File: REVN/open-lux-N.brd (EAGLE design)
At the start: 53 x 68.6 mm, 71 parts, among them IC2 MCP73831, IC3 ATMEGA32U4-AU, IC4 MCP1700-33, J1 AYZ0202, Q1 BSS123, Q4 BSS123, T1 FDN340P, T2 FDN340P, X2 USBSMD, X3 8MHz

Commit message: prettified
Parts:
- moved RIR3 16.1 mm to (3.30, 57.7), turned to 0 degrees
- moved RIR4 15.2 mm to (3.30, 54.9), turned to 180 degrees
- moved Q4 9.66 mm to (22.6, 57.1), turned to 180 degrees
- moved C1 9.21 mm to (19.3, 65.8), turned to 270 degrees
- moved U$7 8.64 mm to (3.56, 47.0)
- moved RC 4.32 mm to (19.3, 61.0), turned to 270 degrees
- moved EEPRM 3.45 mm to (25.7, 65.0), turned to 270 degrees
- moved T1 3.30 mm to (20.8, 11.7), turned to 180 degrees
- moved B1 3.05 mm to (12.7, 64.5)
- moved RD-1 2.97 mm to (37.6, 26.9)
- moved C5 2.40 mm to (44.5, 53.8)
- moved CN1 2.30 mm to (3.81, 35.6)
- moved T2 1.93 mm to (26.2, 11.4)
- moved IC3 1.55 mm to (10.9, 22.9)
- moved C7 1.37 mm to (23.1, 18.0)
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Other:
- board text added: "LUX"
- board text added: "OPEN-"
- board text added: "PUBLICLAB"

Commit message: update
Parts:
- removed J1: AYZ0202, SparkFunNew:AYZ0202
- added J2: EG1206, adafruit:EG1206
- moved C3 42.3 mm to (8.89, 25.7)
- moved IC4 38.2 mm to (8.64, 32.0)
- moved C2 37.0 mm to (8.89, 28.4), turned to 180 degrees
- moved C6 24.2 mm to (2.54, 15.7), turned to 270 degrees
- moved CHARGE 18.2 mm to (32.5, 59.4), turned to 90 degrees
- moved Q1 17.4 mm to (14.2, 31.2)
- moved C7 16.7 mm to (6.60, 15.5)
- moved X3 15.9 mm to (5.08, 20.6), turned to 0 degrees
- moved C9 14.2 mm to (7.11, 2.03)
- moved RE1 9.96 mm to (33.0, 56.6), turned to 180 degrees
- moved RIR3 8.92 mm to (6.35, 66.0), turned to 90 degrees
- moved CN1 8.39 mm to (3.56, 43.9)
- moved IC3 8.18 mm to (18.3, 19.3), turned to 270 degrees
- moved U$7 7.37 mm to (3.56, 54.4)
- moved RIR4 7.18 mm to (4.32, 62.0)
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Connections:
- removed net N$1: J1.3, J1.6
- new net N$16: J2.2
- net VBAT: no longer J1.2, J1.5
- net VDD: now also J2.3; no longer J1.1, J1.4
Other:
- board text added: "PUBLICLAB.ORG"
- board text removed: "PUBLICLAB"

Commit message: update
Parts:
- removed RE2, RE3, RE6: 1.5K, rcl:R0805
- added IRR1, IRR2, IRR5: 1.5K, rcl:R0805
- moved RIR4 11.5 mm to (3.56, 50.5)
- moved IC4 4.38 mm to (7.87, 36.3)
- moved U$7 3.56 mm to (3.56, 57.9)
- moved C2 2.34 mm to (7.37, 30.2), turned to 270 degrees
- moved LUXRGB2 2.18 mm to (42.9, 49.8)
- moved C3 1.55 mm to (7.37, 25.4), turned to 90 degrees
- moved J2 0.80 mm to (2.79, 31.0)
- moved LUXNIR1 0.80 mm to (39.1, 55.4)
- moved B1 0.76 mm to (13.5, 64.5)
- moved C5 0.76 mm to (45.2, 55.6)
- moved RIR3 0.76 mm to (7.11, 66.0)
- moved C4 0.57 mm to (27.2, 36.3), turned to 0 degrees
- moved CHARGE 0.57 mm to (32.0, 59.7)
- moved IR4 0.57 mm to (22.1, 47.2)
- moved EEPRM 0.51 mm to (28.4, 64.8)
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- renumbered RE4 to IRR3, RE5 to IRR4
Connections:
- removed net N$8: IR5.C
- removed net VCC1: RE6.2
- net N$11: now also IRR1.1; no longer RE3.1
- net N$13: now also IRR2.1; no longer RE2.1
- net N$18: now also IRR5.1; no longer RE6.1
- net N$9: now also IR5.C
- net VCC: now also IRR1.2, IRR2.2, IRR5.2; no longer RE2.2, RE3.2

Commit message: update
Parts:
- moved RC 2.34 mm to (22.6, 62.7)
- moved C1 1.93 mm to (22.4, 66.5), turned to 180 degrees
- moved EEPRM 1.80 mm to (30.2, 65.0)
- moved U$1 1.30 mm to (41.1, 63.5)
- moved B1 1.02 mm to (14.5, 64.5)
- moved C5 0.57 mm to (45.0, 55.1)
- moved RIR3 0.25 mm to (6.86, 66.0), turned to 180 degrees

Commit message: update
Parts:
- removed U$7: M04X2, SparkFun-Connectors:2X4
- added JP2: M05X2NO_SILK, SparkFun-Connectors:2X5_NOSILK
- moved RIR4 19.3 mm to (20.6, 59.7)
- moved C6 4.83 mm to (2.54, 20.6)
- moved C7 4.07 mm to (2.54, 15.7), turned to 270 degrees
- moved X3 2.75 mm to (6.60, 18.3), turned to 90 degrees
- moved C3 1.85 mm to (7.87, 27.2)
- moved C2 1.61 mm to (7.87, 31.8)
- moved Q4 1.48 mm to (22.4, 56.4)
- moved CN1 1.30 mm to (3.81, 45.2)
- moved IRG 1.14 mm to (13.0, 58.7)
- moved IRL 1.14 mm to (10.4, 56.1)
- moved EEPRM 1.05 mm to (31.2, 64.8)
- moved IC3 1.05 mm to (17.3, 19.6), turned to 225 degrees
- moved C1 1.05 mm to (23.4, 66.3)
- moved J2 0.92 mm to (3.30, 31.8)
- moved IC4 0.92 mm to (8.64, 36.8)
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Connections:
- net VDD renamed N$1
- removed net N$16: J2.2
- net A0: now also JP2.6; no longer NKA.5, NKA1.6
- net A1: now also B2.1, JP2.8; no longer NKA.4, NKA1.5
- net A2: now also B3.1, JP2.10; no longer NKA.3
- net A3: now also B1.1; no longer NKA.1, NKA1.2
- net A4: now also NKA.1, NKA1.2; no longer B2.1
- net D4: now also NKA.3, NKA1.4; no longer U$7.5
- net D8: now also NKA.5, NKA1.6; no longer B1.1
- net D9: now also NKA.4, NKA1.5; no longer B3.1
- net GND: now also JP2.9; no longer U$7.4
- net RXD: now also JP2.2; no longer U$7.8
- net SCL: now also JP2.3; no longer U$7.3
- net SDA: now also JP2.1; no longer U$7.1
- net TXD: now also JP2.4; no longer U$7.6
- net VBAT: now also J2.2
- net VBUS: now also JP2.5; no longer U$7.7
- net VCC: now also JP2.7
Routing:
- net GND: track 0.00 -> 481.6 mm, vias 0 -> 13
- net VCC: track 0.00 -> 370.3 mm, vias 0 -> 18
- net VBUS: track 0.00 -> 153.1 mm, vias 0 -> 7
- net SCL: track 0.00 -> 129.1 mm, vias 0 -> 7
- net A2: track 0.00 -> 121.5 mm, vias 0 -> 4
- net A1: track 0.00 -> 116.2 mm, vias 0 -> 3
- net VBAT: track 0.00 -> 106.0 mm, vias 0 -> 3
- net SDA: track 0.00 -> 104.5 mm, vias 0 -> 8
- net D5: track 0.00 -> 74.5 mm, vias 0 -> 2
- net A0: track 0.00 -> 74.4 mm, vias 0 -> 4
- net RESET: track 0.00 -> 69.0 mm, vias 0 -> 4
- net MISO: track 0.00 -> 67.5 mm, vias 0 -> 5
- net A3: track 0.00 -> 67.5 mm, vias 0 -> 6
- net D6: track 0.00 -> 62.4 mm, vias 0 -> 4
- net N$9: track 0.00 -> 55.8 mm, vias 0 -> 6
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
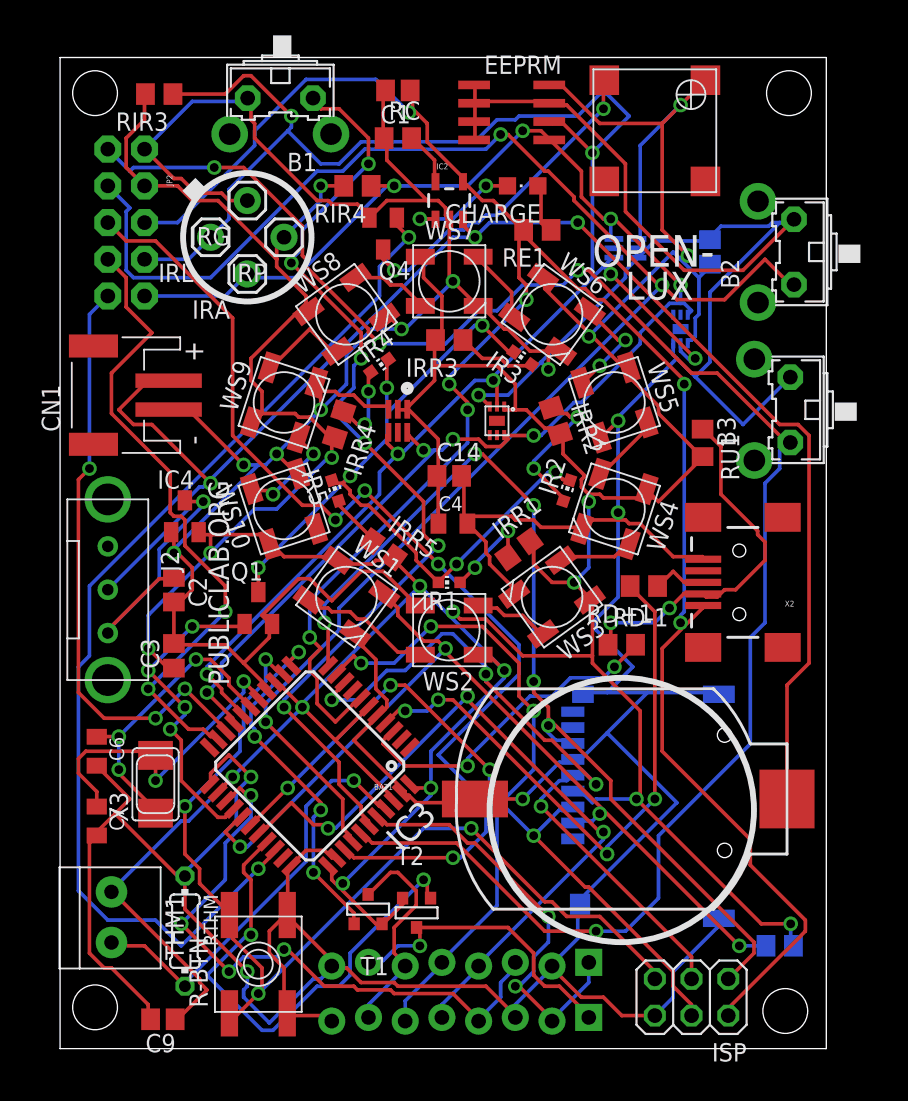
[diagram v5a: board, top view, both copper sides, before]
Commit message: fully routed
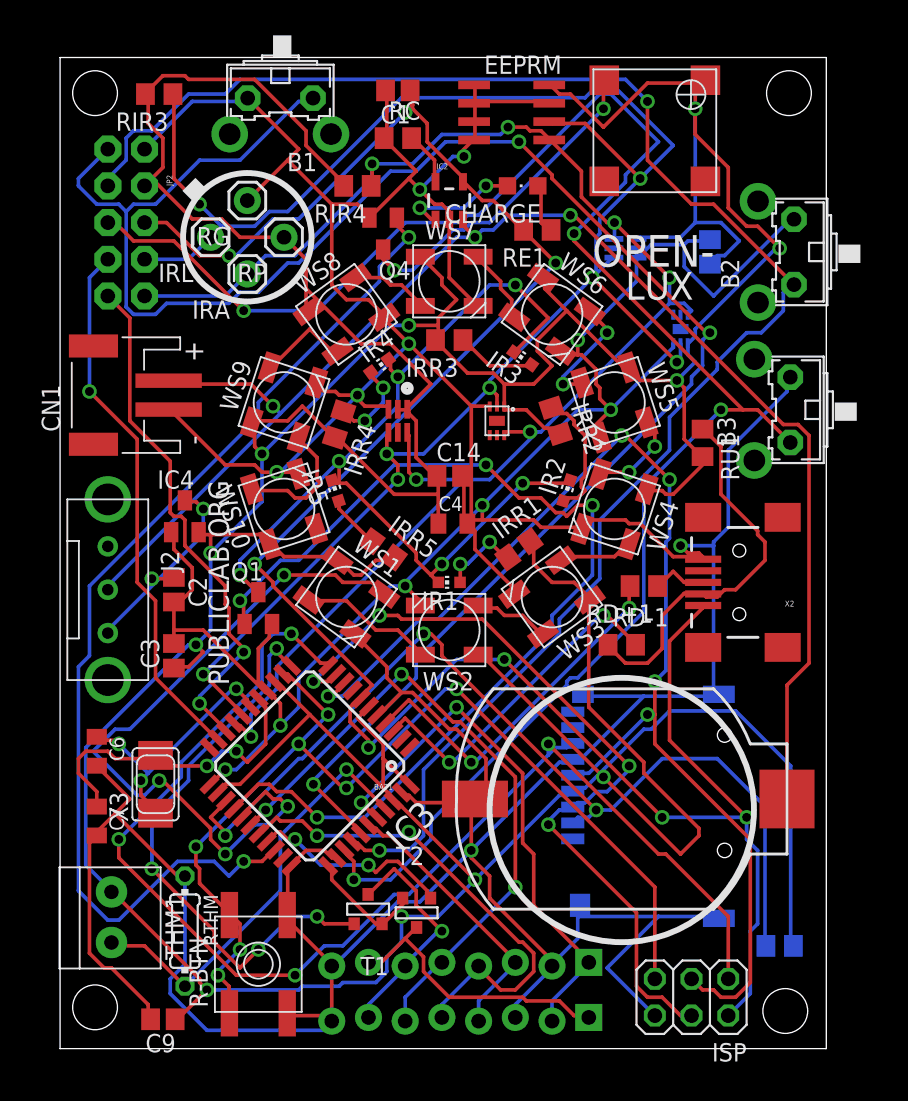
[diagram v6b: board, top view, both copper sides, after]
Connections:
- net A0: now also B3.1
- net A2: now also B1.1; no longer B3.1
- net A3: now also NKA.3, NKA1.4; no longer B1.1
- net D4: now also MICROSD.2, RSD.1; no longer NKA.3, NKA1.4
- net D6: no longer MICROSD.2, RSD.1
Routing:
- net VCC: track 370.3 -> 441.8 mm, vias 18 -> 11
- net A0: track 74.4 -> 126.9 mm
- net A3: track 67.5 -> 19.2 mm, vias 6 -> 0
- net D12: track 22.4 -> 70.6 mm
- net SCK: track 48.8 -> 84.3 mm, vias 4 -> 5
- net D4: track 43.0 -> 66.7 mm, vias 4 -> 3
- net MISO: track 67.5 -> 88.6 mm, vias 5 -> 4
- net D10: track 34.9 -> 14.4 mm
- net GND: track 481.6 -> 464.8 mm
- net D9: track 50.7 -> 34.5 mm, vias 3 -> 2
- net N$21: track 41.3 -> 25.3 mm, vias 4 -> 2
- net D11: track 24.9 -> 39.4 mm
- net D6: track 62.4 -> 49.2 mm
- net N$9: track 55.8 -> 64.0 mm
- net A4: track 29.3 -> 37.5 mm
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
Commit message: update
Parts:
- turned IR2 to 162 degrees
- turned IR3 to 234 degrees
- turned WS1 to 144 degrees
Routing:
- net VCC: track 441.8 -> 372.2 mm, vias 11 -> 16
- net A2: track 128.8 -> 79.7 mm, vias 3 -> 2
- net MOSI: track 55.8 -> 104.2 mm, vias 4 -> 2
- net SCK: track 84.3 -> 37.9 mm, vias 5 -> 2
- net D12: track 70.6 -> 26.7 mm, vias 4 -> 2
- net GND: track 464.8 -> 504.2 mm, vias 13 -> 12
- net MISO: track 88.6 -> 50.1 mm
- net N$3: track 18.3 -> 51.3 mm, vias 3 -> 2
- net D6: track 49.2 -> 25.3 mm, vias 4 -> 2
- net RXD: track 36.3 -> 57.2 mm
- net SCL: track 132.2 -> 152.4 mm
- net A1: track 115.0 -> 133.7 mm
- net SDA: track 107.8 -> 123.7 mm, vias 7 -> 10
- net A4: track 37.5 -> 24.9 mm, vias 2 -> 0
- net D10: track 14.4 -> 26.8 mm, vias 2 -> 4
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
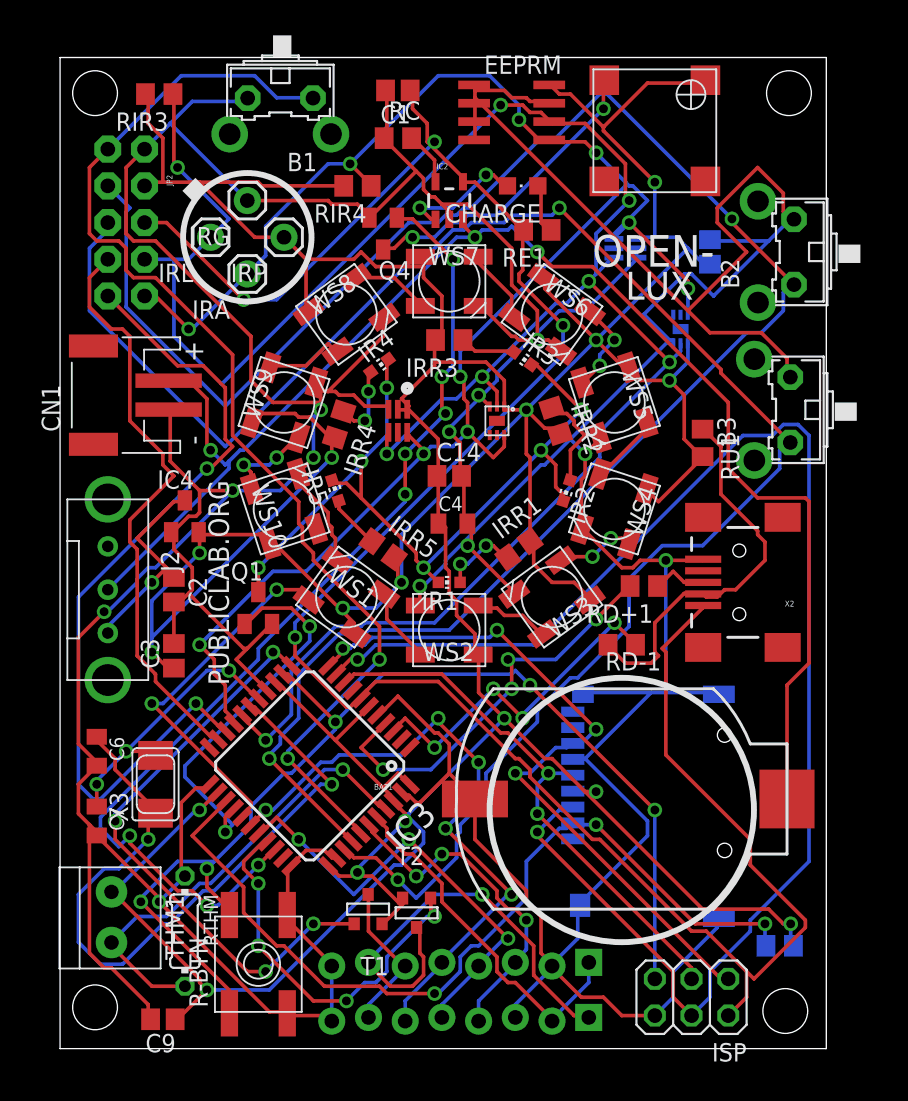
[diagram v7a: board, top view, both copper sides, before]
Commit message: fully routed
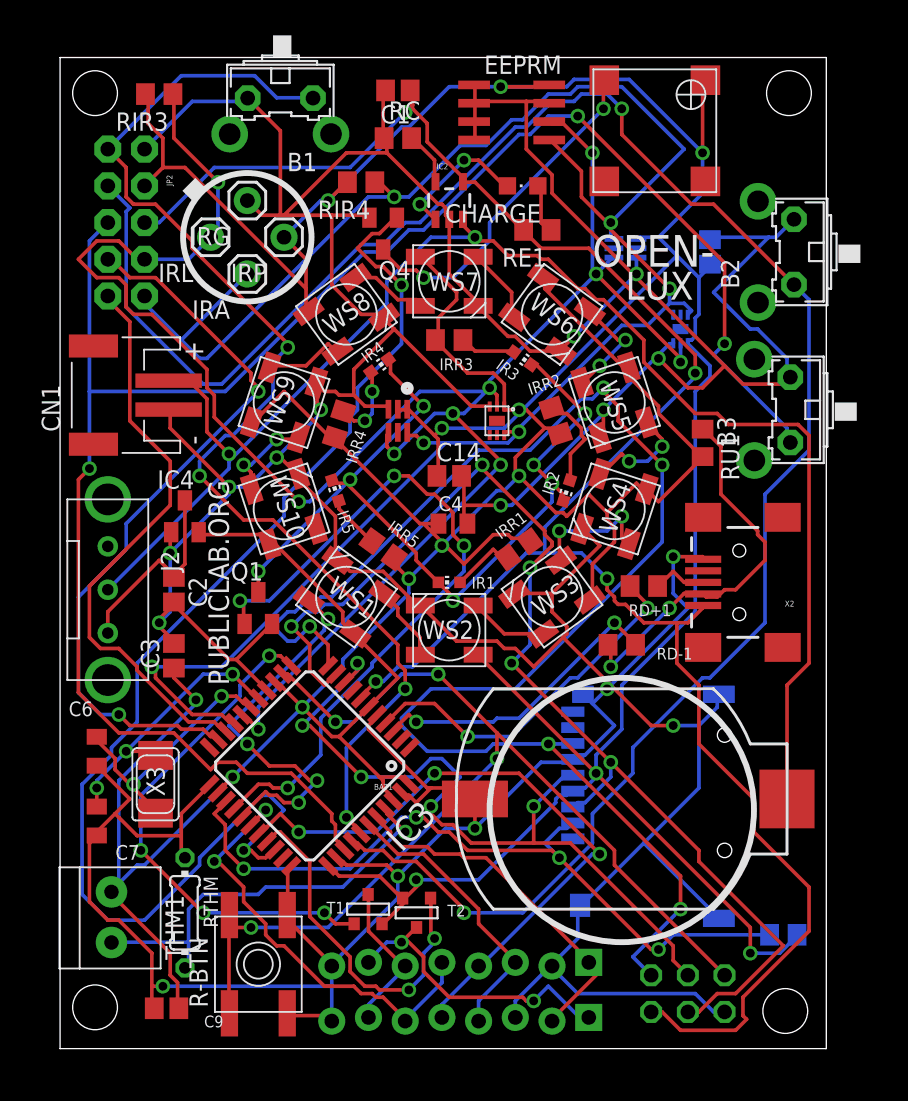
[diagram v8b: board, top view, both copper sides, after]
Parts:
- moved RTHM 1.27 mm to (8.64, 9.40)
- moved C9 0.80 mm to (7.37, 2.79)
- moved RSD 0.80 mm to (50.0, 7.87)
- moved ISP 0.36 mm to (43.4, 3.81), flipped to the bottom
- moved RIR4 0.36 mm to (20.8, 59.9)
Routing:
- net MISO: track 50.1 -> 106.8 mm, vias 4 -> 5
- net VCC: track 372.2 -> 418.2 mm, vias 16 -> 14
- net GND: track 504.2 -> 468.0 mm, vias 12 -> 16
- net N$3: track 51.3 -> 18.1 mm
- net D12: track 26.7 -> 50.0 mm, vias 2 -> 4
- net MOSI: track 104.2 -> 81.2 mm, vias 2 -> 5
- net SDA: track 123.7 -> 141.1 mm, vias 10 -> 6
- net VBUS: track 158.2 -> 140.8 mm
- net RXD: track 57.2 -> 40.0 mm, vias 2 -> 0
- net SCK: track 37.9 -> 53.8 mm, vias 2 -> 5
- net D8: track 44.2 -> 30.5 mm, vias 5 -> 2
- net D9: track 31.8 -> 44.9 mm
- net D5: track 71.6 -> 84.6 mm, vias 8 -> 2
- net TXD: track 40.6 -> 51.6 mm, vias 0 -> 2
- net SCL: track 152.4 -> 141.5 mm, vias 8 -> 10
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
